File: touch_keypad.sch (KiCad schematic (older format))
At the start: 37 parts, among them J1 USB_B_Micro, J18 Conn_01x02_Female, J4 Conn_01x05_Female, J5 Conn_01x04_Female, SW1 SW_Push, SW2 SW_Push, SW3 SW_Push, SW4 SW_Push, SW5 SW_Push, U1 AMS1117-3.3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

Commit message: aq
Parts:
- removed C16, C17, C18: C, Capacitor_SMD:C_0603_1608Metric_Pad1.05x0.95mm_HandSolder, symbol Device:C
- removed J18: Conn_01x02_Female, TerminalBlock:TerminalBlock_Altech_AK300-2_P5.00mm, symbol Connector:Conn_01x02_Female
- removed J4: Conn_01x05_Female, Connector_PinSocket_2.54mm:PinSocket_1x05_P2.54mm_Horizontal, symbol Connector:Conn_01x05_Female
- removed R11, R12, R13: R, Resistor_SMD:R_0603_1608Metric_Pad1.05x0.95mm_HandSolder, symbol Device:R
- added D2: LED, LED_SMD:LED_0603_1608Metric, symbol Device:LED
- added R6: R, Resistor_SMD:R_0603_1608Metric_Pad1.05x0.95mm_HandSolder, symbol Device:R
- added SW10, SW12, SW13, SW15, SW16, SW17, SW7, SW8, SW9: SW_Push, touch_keypad:TouchSlider-2_10x10mm, symbol Switch:SW_Push
- added SW11, SW14, SW6: SW_Push, touch_keypad:cap_button, symbol Switch:SW_Push
- SW3, SW4, SW5: footprint Button_Switch_SMD:SW_Push_1P1T_NO_6x6mm_H9.5mm -> touch_keypad:cap_button
- gave numbers to parts that had none: 1
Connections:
- net Button1: now also SW5.1, SW10.1, SW15.1, SW7.1; no longer C14.1, R10.2, SW2.2
- net Button2: now also SW3.1, SW12.1, SW16.1, SW8.1; no longer SW5.2
- net Button3: now also SW4.1, SW13.1, SW17.1, SW9.1; no longer SW4.2
- net Button4: now also SW6.1, SW7.2, SW8.2, SW9.2
- net Button5: now also SW10.2, SW11.1, SW12.2, SW13.2
- net Button6: now also SW14.1, SW15.2, SW16.2, SW17.2
- net Button7: now also C14.1, R10.2, SW2.2
- net GND: now also D2.1 (K); no longer SW3.1, SW4.1, SW5.1
- net LED: now also R6.2
- net LCD_RST: no longer names the net of SW3.2
- new net: D2.2 (A), R6.1
- no-connect marks 0 -> 6
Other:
- moved on the sheet: C14, C4, C5, C7, C9, D1, J5, R10, R3, SW2, U1

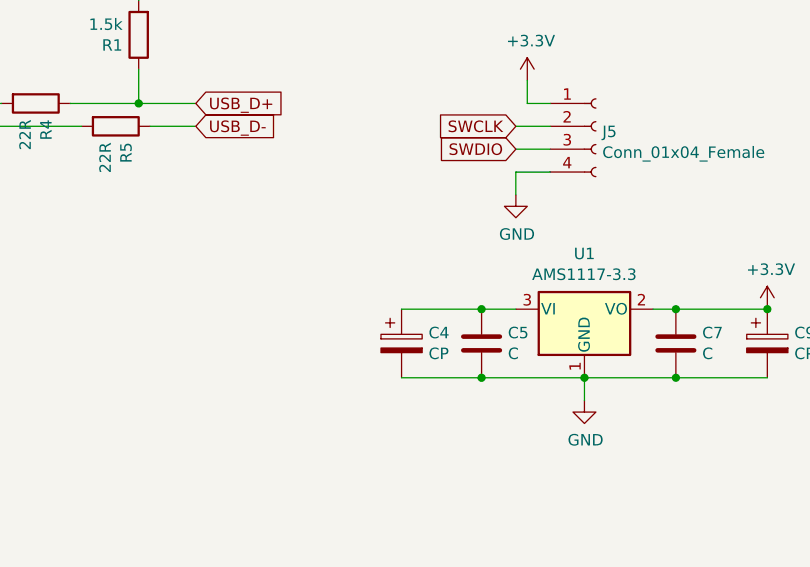
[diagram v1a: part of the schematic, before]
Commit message: upgrade to kicad 6
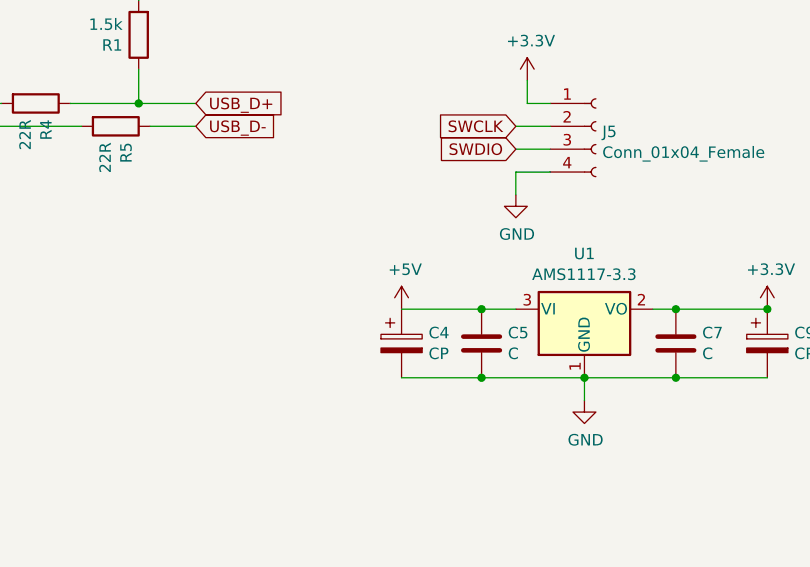
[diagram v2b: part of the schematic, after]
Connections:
- net +5V: now also C4.1, C5.1, U1.3 (VI)
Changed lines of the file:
@@
 	8000 3800 8000 4250
 Connection ~ 7900 3300
+$Comp
+L power:+5V #PWR?
+U 1 1 5F5A334C
+P 3850 6050
+F 0 "#PWR?" H 3850 5900 50  0001 C CNN
+F 1 "+5V" H 3865 6223 50  0000 C CNN
+F 2 "" H 3850 6050 50  0001 C CNN
+F 3 "" H 3850 6050 50  0001 C CNN
+	1    3850 6050
+	1    0    0    -1
+$EndComp
 $EndSCHEMATC
